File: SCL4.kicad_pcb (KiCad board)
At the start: 2 copper layers, 150.5 x 233.3 mm, 49 parts, among them J1 TSPARE1, J11 Conn_01x10_Male, J2 TSPARE2, J3 Siemens_A1010-A263, J4 TSPARE3, J5 SPARE1, J7 5V out, J8 SPARE2, J9 SPARE3, U1 MC3487DX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

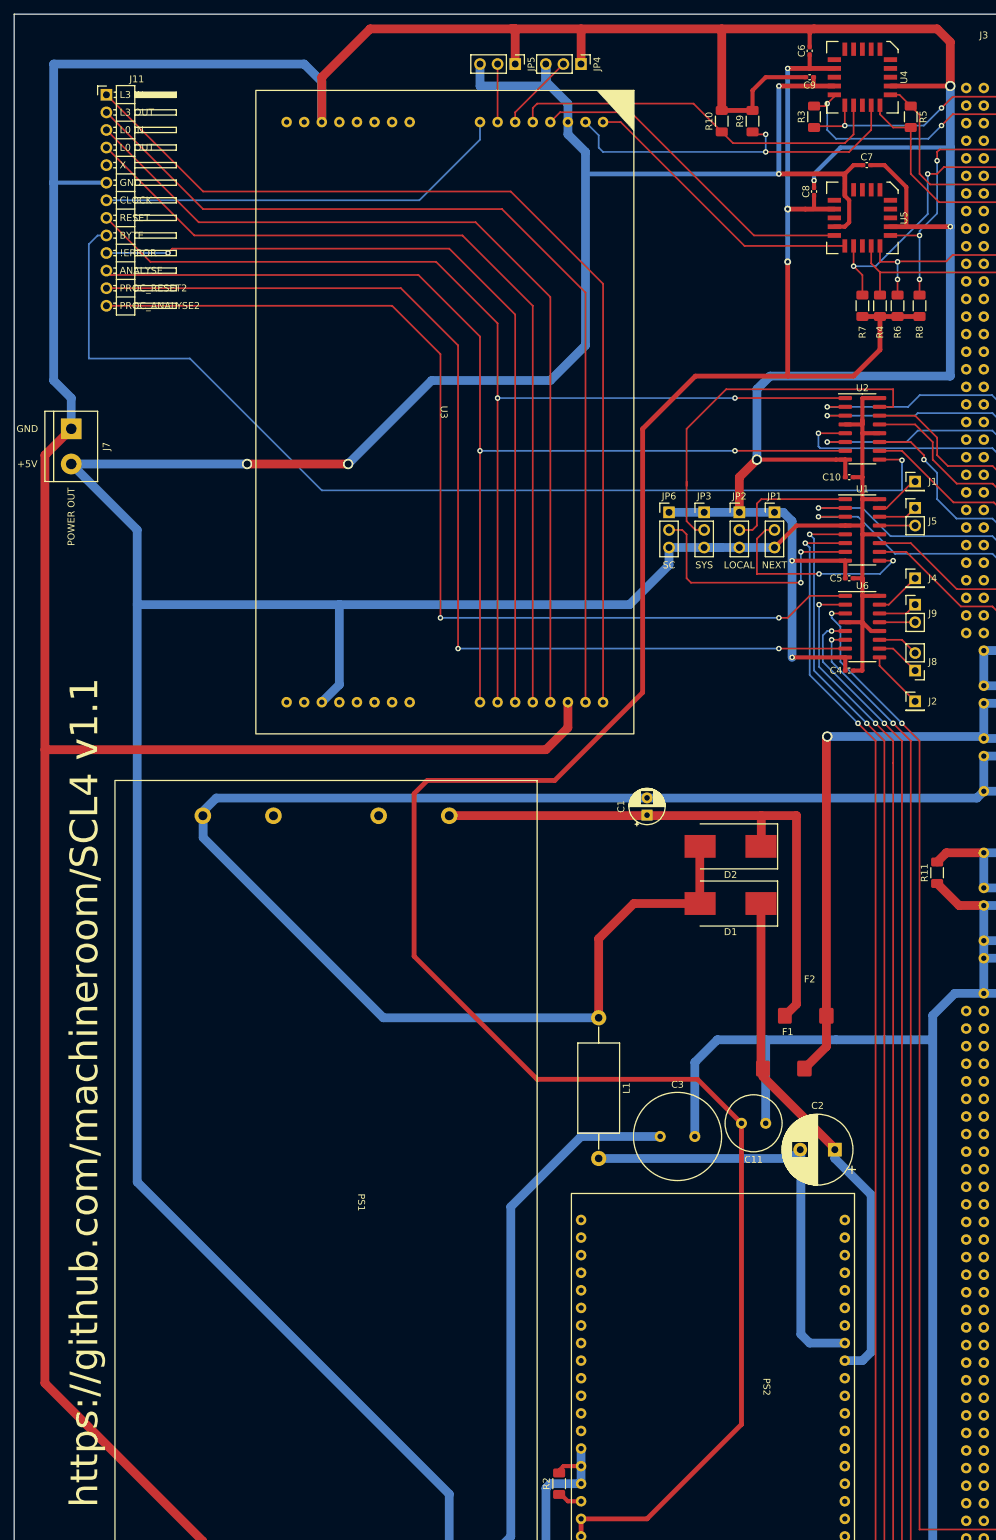
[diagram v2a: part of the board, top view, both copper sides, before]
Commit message: Use RJ45 external and add thermal pads
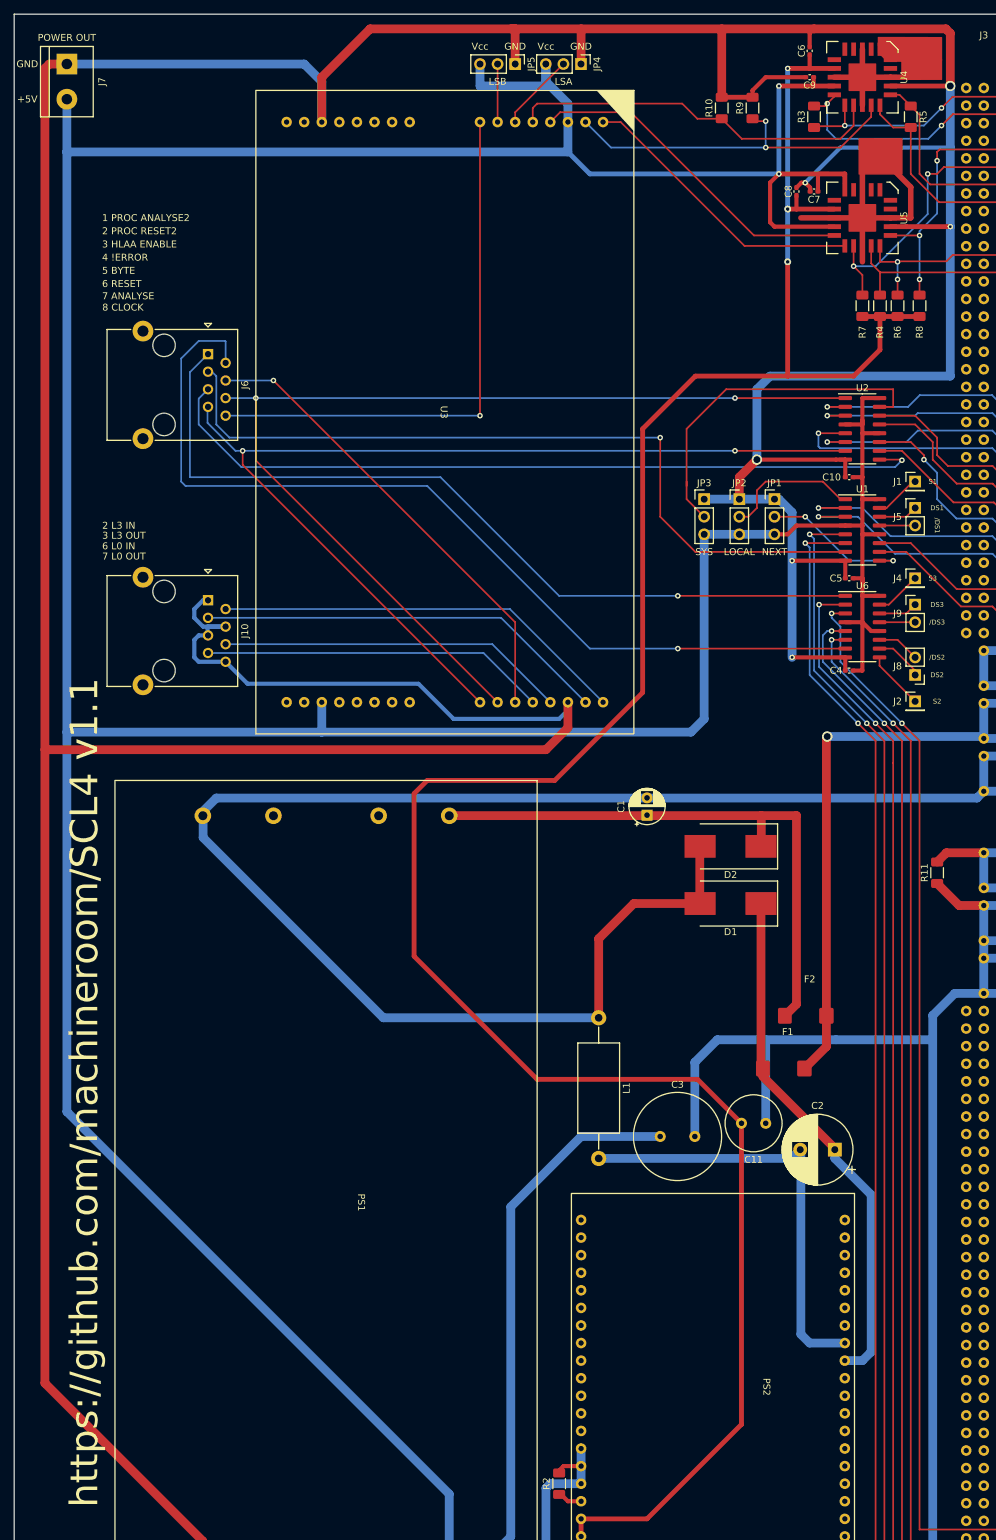
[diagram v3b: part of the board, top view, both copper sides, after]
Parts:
- removed J11: Conn_01x10_Male, Connector_PinHeader_2.54mm:PinHeader_1x13_P2.54mm_Horizontal
- removed JP6: SC MODE, Connector_PinHeader_2.54mm:PinHeader_1x03_P2.54mm_Vertical
- added J10: 8P8C, Connector_RJ:RJ45_Ninigi_GE, F.Cu at (182.3, 101.0)
- added J6: 8P8C, Connector_RJ:RJ45_Ninigi_GE, F.Cu at (182.3, 65.4)
- moved J7 52.7 mm to (161.9, 23.5)
- moved C7 8.52 mm to (269.9, 41.9), turned to 180 degrees
- moved C8 2.54 mm to (267.3, 41.9)
- moved JP1 1.91 mm to (264.2, 86.4)
- moved JP2 1.91 mm to (259.1, 86.4)
- moved JP3 1.91 mm to (254.0, 86.4)
- moved R10 1.91 mm to (256.5, 29.8)
- moved R9 1.91 mm to (261.0, 29.8)
- moved J8 0.63 mm to (284.5, 111.8)
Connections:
- U1 pad 7: Net-(JP6-Pad2) -> /THLAA_ENABLE
- U4 pad 1: unconnected-(U4-Pad1) -> thermal1
- U4 pad 11: unconnected-(U4-Pad11) -> thermal1
- U4 pad 16: unconnected-(U4-Pad16) -> thermal1
- U4 pad 3: unconnected-(U4-Pad3) -> thermal1
- U4 pad 4: unconnected-(U4-Pad4) -> thermal1
- U4 pad 6: unconnected-(U4-Pad6) -> thermal1
- U5 pad 1: unconnected-(U5-Pad1) -> thermal2
- U5 pad 11: unconnected-(U5-Pad11) -> thermal2
- U5 pad 16: unconnected-(U5-Pad16) -> thermal2
- U5 pad 6: unconnected-(U5-Pad6) -> thermal2
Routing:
- net /THLAA_ENABLE: track 0.00 -> 113.6 mm, vias 0 -> 1
- net /TL3In: track 143.5 -> 60.1 mm
- net /TL0In: track 132.7 -> 50.4 mm
- net /TL3Out: track 139.2 -> 59.6 mm
- net /TL0Out: track 128.3 -> 49.9 mm
- net /TNotError: track 119.3 -> 67.9 mm
- net GND: track 1116.9 -> 1166.7 mm
- net +5V: track 678.5 -> 726.6 mm, vias 4 -> 2
- net /TByte: track 152.6 -> 113.5 mm
- net thermal2: track 0.00 -> 37.2 mm
- net Net-(JP6-Pad2): track 36.8 -> 0.00 mm, vias 2 -> 0
- net thermal1: track 0.00 -> 32.9 mm
- net /TPROC_ANALYSE2: track 149.1 -> 120.6 mm, vias 2 -> 1
- net /TReset: track 167.8 -> 147.9 mm
- net /TPROC_RESET2: track 154.0 -> 134.3 mm, vias 2 -> 1
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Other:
- board text added: "/DS1"
- board text added: "/DS2"
- board text added: "/DS3"
- board text added: "1 PROC ANALYSE2"
- board text added: "2 L3 IN"
- board text added: "2 PROC RESET2"
- board text added: "3 HLAA ENABLE"
- board text added: "3 L3 OUT"
- board text added: "4 !ERROR"
- board text added: "5 BYTE"
- board text added: "6 L0 IN"
- board text added: "6 RESET"
- board text added: "7 ANALYSE"
- board text added: "7 L0 OUT"
- board text added: "8 CLOCK"
- board text added: "DS1"
- board text added: "DS2"
- board text added: "DS3"
- board text added: "LSA"
- board text added: "LSB"
- board text added: "S1"
- board text added: "S2"
- board text added: "S3"
- board text added: "Vcc"
- board text removed: "!ERROR"
- board text removed: "ANALYSE"
- board text removed: "BYTE"
- board text removed: "CLOCK"
- board text removed: "L0 IN"
- board text removed: "L0 OUT"
- board text removed: "L3 IN"
- board text removed: "L3 OUT"
- board text removed: "PROC_ANALYSE2"
- board text removed: "PROC_RESET2"
- board text removed: "RESET"
- board text removed: "SC"
- board text removed: "X"

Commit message: Add extraction holes
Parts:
- added ?: , , F.Cu at (156.2, 247.7)
- added ?: , , F.Cu at (156.2, 18.4)
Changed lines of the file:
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@@
     )
+  )
+  (footprint "" (layer "F.Cu")
+    (at 156.21 247.65)
+    (fp_text reference "" (at 0 0) (layer "F.SilkS")
+      (effects (font (size 1.27 1.27) (thickness 0.15)))
+    )
+    (fp_text value "" (at 0 0) (layer "F.SilkS")
+      (effects (font (size 1.27 1.27) (thickness 0.15)))
+    )
+    (pad "" np_thru_hole circle (at 0 0) (size 2.8 2.8) (drill 2.8) (layers F&B.Cu *.Mask)
+      (zone_connect 0))
   )
   (footprint "Capacitor_SMD:C_0402_1005Metric_Pad0.74x0.62mm_HandSolder" (layer "F.Cu")
@@
     )
   )
+  (footprint "" (layer "F.Cu")
+    (at 156.21 18.415)
+    (fp_text reference "" (at 0 0) (layer "F.SilkS")
+      (effects (font (size 1.27 1.27) (thickness 0.15)))
+    )
+    (fp_text value "" (at 0 0) (layer "F.SilkS")
+      (effects (font (size 1.27 1.27) (thickness 0.15)))
+    )
+    (pad "" np_thru_hole circle (at 0 0) (size 2.8 2.8) (drill 2.8) (layers F&B.Cu *.Mask)
+      (zone_connect 0))
+  )
   (footprint "Package_SO:SOIC-16_3.9x9.9mm_P1.27mm" (layer "F.Cu")

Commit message: more LEDs
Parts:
- added D3: 5V OK, LED_THT:LED_Rectangular_W5.0mm_H2.0mm, F.Cu at (167.0, 41.9)
- added D4: -5V OK, LED_THT:LED_Rectangular_W5.0mm_H2.0mm, F.Cu at (167.0, 45.7)
- added D5: Reset, LED_THT:LED_Rectangular_W5.0mm_H2.0mm, F.Cu at (167.0, 53.3)
- added D6: Error, LED_THT:LED_Rectangular_W5.0mm_H2.0mm, F.Cu at (167.0, 49.5)
- added R1: 220R, Resistor_SMD:R_1206_3216Metric_Pad1.30x1.75mm_HandSolder, F.Cu at (174.6, 41.9)
- added R12: 220R, Resistor_SMD:R_1206_3216Metric_Pad1.30x1.75mm_HandSolder, F.Cu at (174.6, 45.7)
- added R13: 220R, Resistor_SMD:R_1206_3216Metric_Pad1.30x1.75mm_HandSolder, F.Cu at (174.6, 53.3)
- added R14: 220R, Resistor_SMD:R_1206_3216Metric_Pad1.30x1.75mm_HandSolder, F.Cu at (174.6, 49.5)
- moved C2 3.98 mm to (276.9, 180.3)
- moved C11 1.27 mm to (264.2, 176.5)
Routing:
- net -5V: track 349.3 -> 461.0 mm
- net /TNotError: track 67.9 -> 106.7 mm
- net GND: track 1166.7 -> 1195.6 mm
- net /TReset: track 147.9 -> 176.8 mm
- net +5V: track 726.6 -> 742.5 mm, vias 2 -> 3
- net Net-(D6-Pad2): track 0.00 -> 3.53 mm
- net Net-(D5-Pad2): track 0.00 -> 3.53 mm
- net Net-(D4-Pad2): track 0.00 -> 3.53 mm
- net Net-(D3-Pad2): track 0.00 -> 3.53 mm
- net Net-(C2-Pad2): track 63.2 -> 64.1 mm
- net Net-(C2-Pad1): track 75.7 -> 76.2 mm
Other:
- board text added: "-5V OK"
- board text added: "1 GND 2 L3 IN 3 L3 OUT 4 GND 5 GND 6 L0 IN 7 L0 OUT 8 GND"
- board text added: "1 PROC ANAL2 2 PROC RESET2 3 HLAA ENABLE 4 !ERROR 5 BYTE 6 RESET 7 ANALYSE 8 CLOCK"
- board text added: "5V OK"
- board text added: "ERROR"
- board text added: "RESET"
- board text removed: "1 PROC ANALYSE2"
- board text removed: "2 L3 IN"
- board text removed: "2 PROC RESET2"
- board text removed: "3 HLAA ENABLE"
- board text removed: "3 L3 OUT"
- board text removed: "4 !ERROR"
- board text removed: "5 BYTE"
- board text removed: "6 L0 IN"
- board text removed: "6 RESET"
- board text removed: "7 ANALYSE"
- board text removed: "7 L0 OUT"
- board text removed: "8 CLOCK"

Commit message: tidy
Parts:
- moved J7 1.90 mm to (161.9, 25.4)
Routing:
- net -5V: track 461.0 -> 472.9 mm
- net GND: track 1195.6 -> 1193.0 mm
- net +5V: track 742.5 -> 740.5 mm
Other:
- board text added: "Designed Christmas 2022 Dedicated to Karla, Zak & Sam!"
- board text added: "github.com/machineroom/SCL4 v1.1"
- board text removed: "https://github.com/machineroom/SCL4 v1.1"
